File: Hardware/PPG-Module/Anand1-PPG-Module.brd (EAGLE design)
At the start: 100 x 80 mm, 0 parts

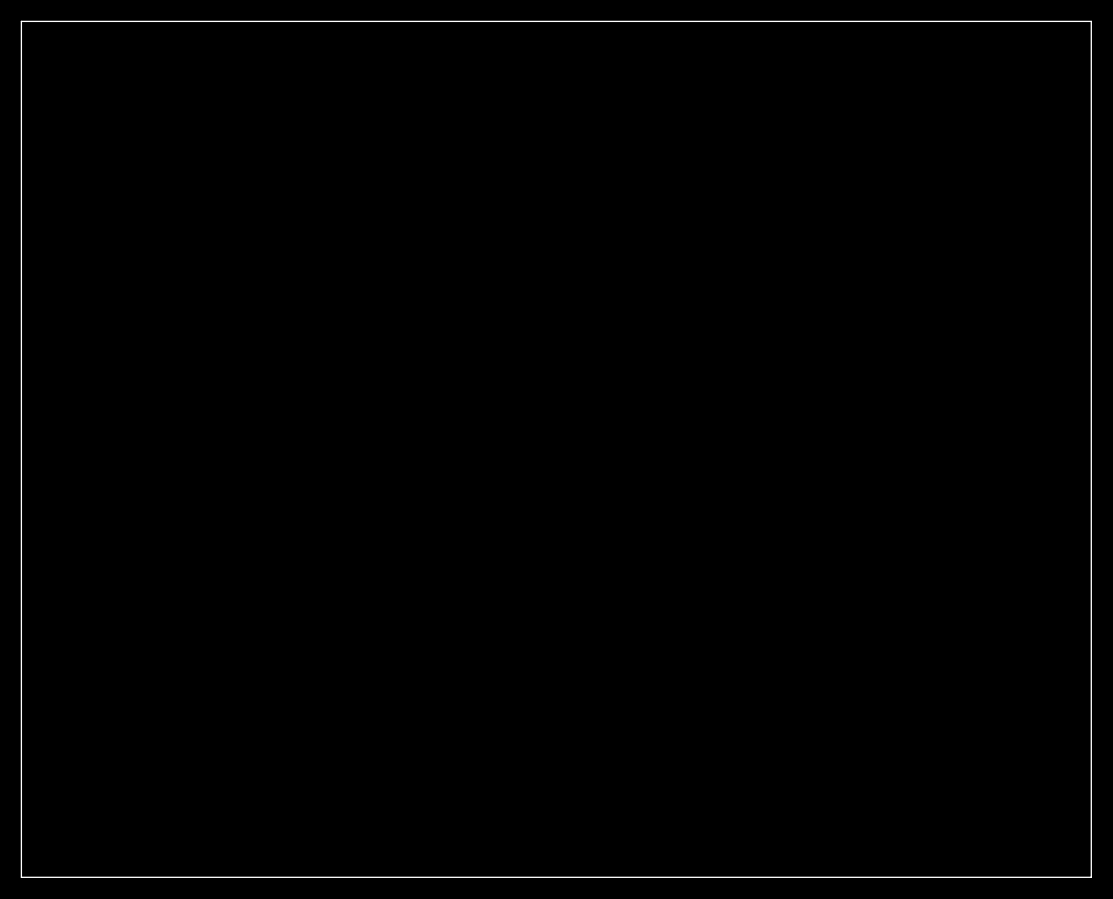
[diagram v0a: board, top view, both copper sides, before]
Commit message: added PPG Module board, BOM, and gitignore
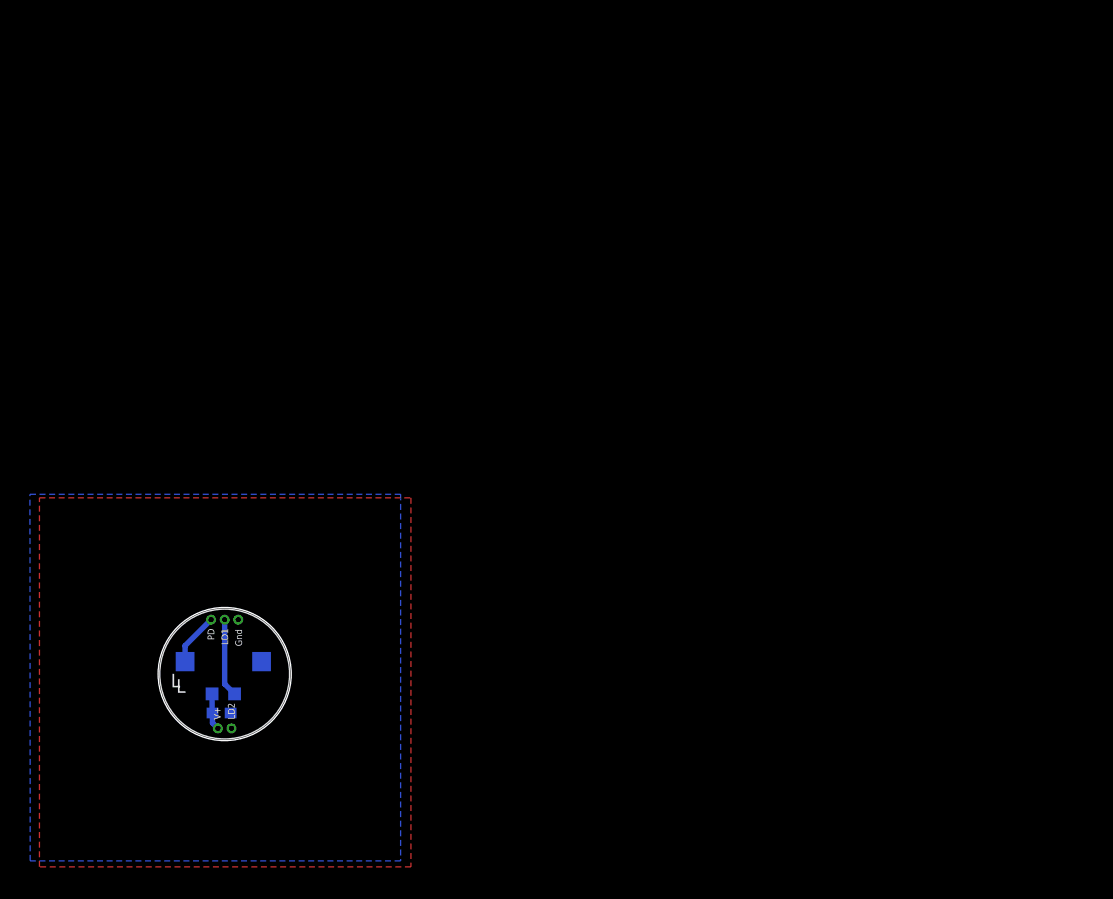
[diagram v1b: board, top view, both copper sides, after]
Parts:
- added C1: 2.2u, CalvEngIO-Passives:C0603
- added J1: (no value), LinnesLab-Connectors:PPG.MODULE.2
- added LED1: (no value), LinnesLab-LED:LED-0805
- added PD: (no value), CalvEngIO-Sensors:2-SMD.GULLWING
- added U$3: LINNES.LAB.LOGO, CalvEngIO-Logos:LINNES.LAB.LOGO
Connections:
- new net GND: C1.2, J1.GND, PD.+
- new net LED.C: J1.LD1, LED1.C
- new net PD.C: J1.PD, PD.-
- new net V+: C1.1, J1.V+, LED1.A
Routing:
- net LED.C: track 0.00 -> 7.32 mm
- net PD.C: track 0.00 -> 4.92 mm
- net V+: track 0.00 -> 3.47 mm
- added copper zone on layer 1, net GND
- added copper zone on layer 16, net GND
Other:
- board size 100 x 80 mm -> 12.4 x 12.4 mm
